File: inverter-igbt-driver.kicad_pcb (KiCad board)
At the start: 2 copper layers, 79 x 32 mm, 36 parts, among them J1 Conn_01x06, U1 NE555, U2 IXDF604SIA, U3 FOD8316, U6 Transformer_2P_2S

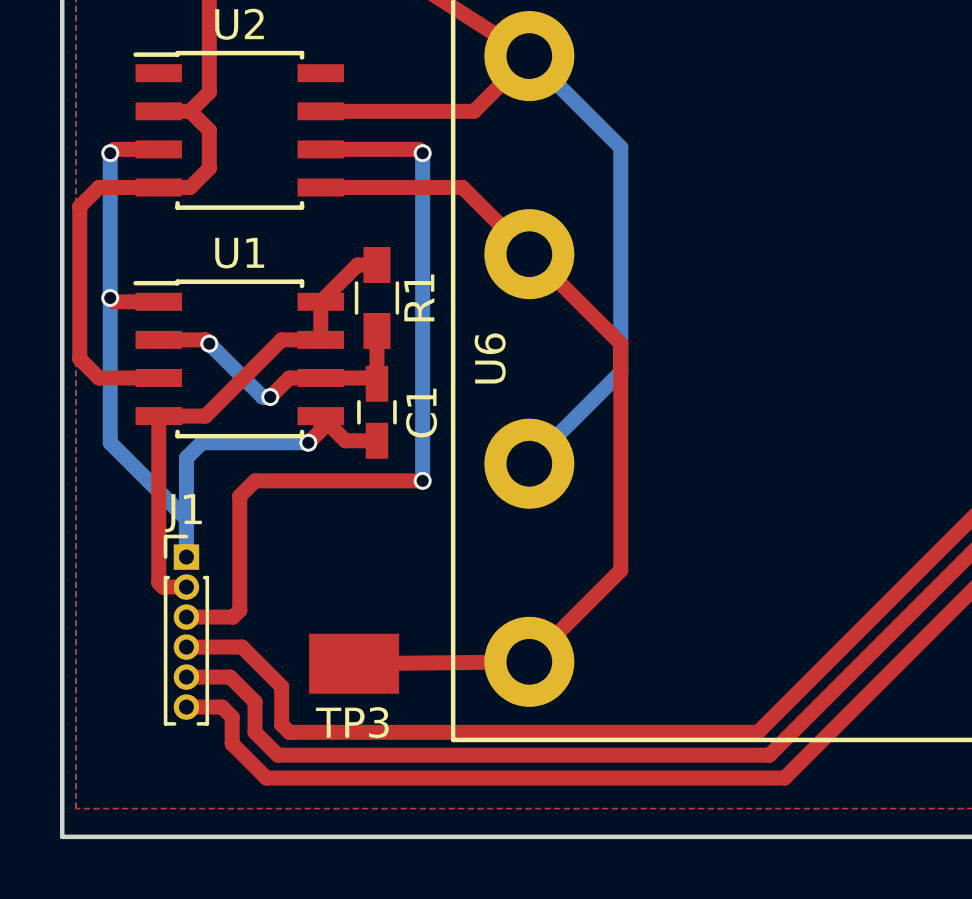
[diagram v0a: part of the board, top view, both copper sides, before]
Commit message: Adds pull-down resistors for logic nets.
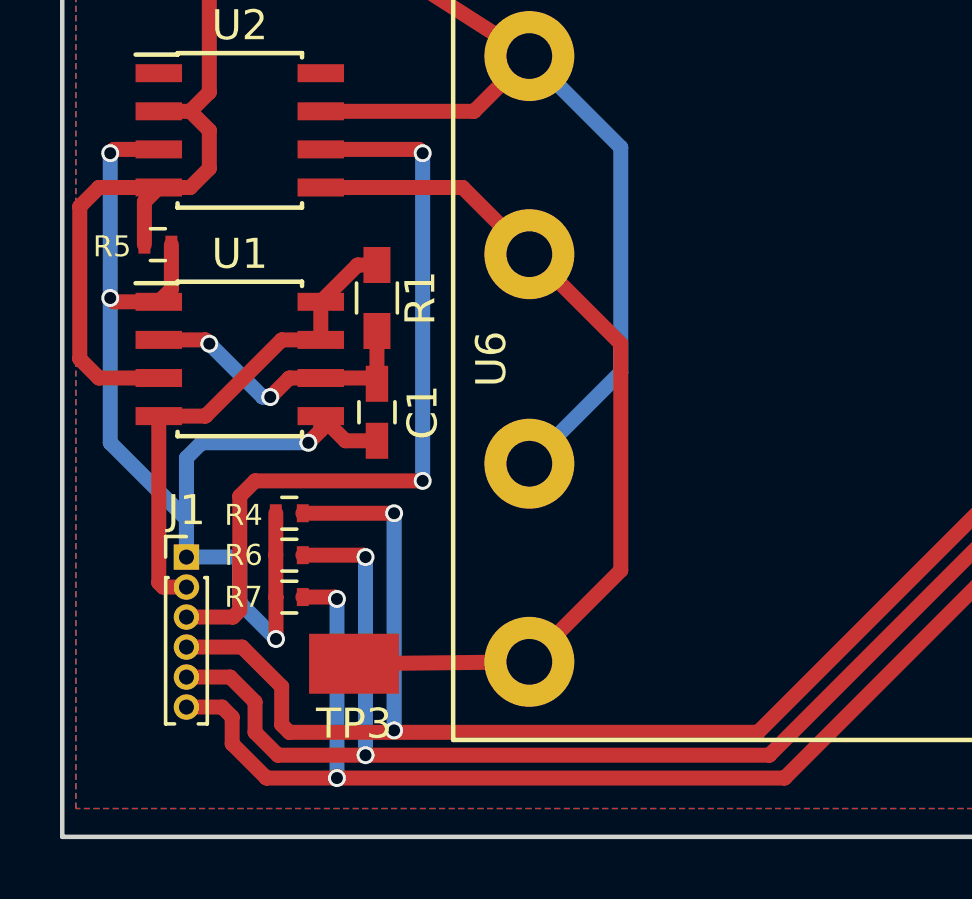
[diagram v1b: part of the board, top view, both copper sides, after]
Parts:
- added R4: 1k, Resistors_SMD:R_0402, F.Cu at (107.6, 57.2)
- added R5: 1k, Resistors_SMD:R_0402, F.Cu at (103.2, 48.3)
- added R6: 1k, Resistors_SMD:R_0402, F.Cu at (107.6, 58.6)
- added R7: 1k, Resistors_SMD:R_0402, F.Cu at (107.6, 60.0)
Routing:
- net GND: track 41.1 -> 52.4 mm, vias 6 -> 7
- net /VIN: track 59.9 -> 70.3 mm, vias 0 -> 2
- net /FAULT: track 59.0 -> 67.7 mm, vias 0 -> 2
- net /RESET: track 58.0 -> 65.3 mm, vias 2 -> 4
- net Net-(R5-Pad1): track 23.1 -> 25.2 mm

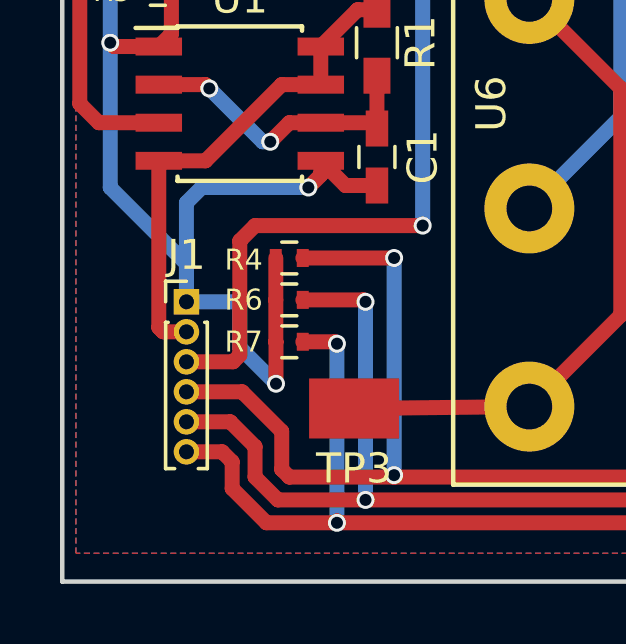
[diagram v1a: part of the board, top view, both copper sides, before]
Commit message: Add GND test point.
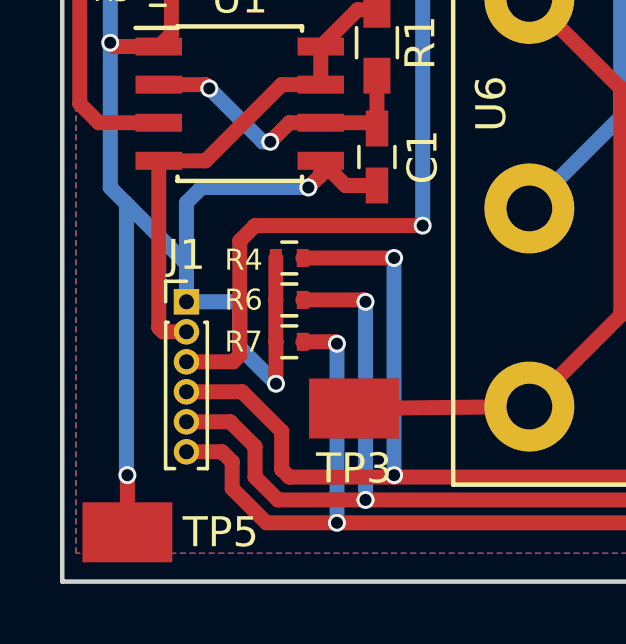
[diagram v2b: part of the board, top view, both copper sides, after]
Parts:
- added TP5: TEST, inverter-igbt-driver:TP RCT (0805), F.Cu at (102.2, 66.4)
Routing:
- net GND: track 52.4 -> 63.4 mm, vias 7 -> 8
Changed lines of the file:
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@@
 (kicad_pcb (version 4) (host pcbnew 4.0.7)
   (general
-    (links 80)
+    (links 81)
     (no_connects 2)
     (area 99.924999 35.924999 179.075001 68.075001)
     (thickness 1.6)
     (drawings 4)
-    (tracks 220)
+    (tracks 225)
     (zones 0)
-    (modules 40)
+    (modules 41)
     (nets 26)
   )
@@
     )
   )
+  (module "inverter-igbt-driver:TP RCT (0805)" (layer F.Cu)
+    (at 102.1715 66.3575)
+    (fp_text reference TP5 (at 3.1115 0) (layer F.SilkS)
+      (effects (font (size 1 1) (thickness 0.15)))
+    )
+    (fp_text value TEST (at 0 -2.25) (layer F.Fab) hide
+      (effects (font (size 1 1) (thickness 0.15)))
+    )
+    (pad 1 smd rect (at 0 0) (size 3 2) (layers F.Cu F.Paste F.Mask)
+      (net 2 GND))
+  )
   (gr_line (start 100 68) (end 100 36) (angle 90) (layer Edge.Cuts) (width 0.15))
   (gr_line (start 179 68) (end 100 68) (angle 90) (layer Edge.Cuts) (width 0.15))
@@
   (segment (start 110.49 51.138) (end 110.49 52.898) (width 0.5) (layer F.Cu) (net 1))
   (segment (start 110.49 52.898) (end 110.297 52.705) (width 0.5) (layer F.Cu) (net 1))
+  (segment (start 102.1715 66.3575) (end 102.1715 64.4525) (width 0.5) (layer F.Cu) (net 2) (status 400000))
+  (segment (start 102.13975 64.42075) (end 102.13975 55.40375) (width 0.5) (layer B.Cu) (net 2))
+  (segment (start 102.1715 64.4525) (end 102.13975 64.42075) (width 0.5) (layer B.Cu) (net 2))
+  (via (at 102.1715 64.4525) (size 0.6) (drill 0.4) (layers F.Cu B.Cu) (net 2))
   (segment (start 103.6375 48.26) (end 103.6375 49.7455) (width 0.5) (layer F.Cu) (net 2))
   (segment (start 103.6375 49.7455) (end 103.218 50.165) (width 0.5) (layer F.Cu) (net 2))
@@
   (segment (start 104.14 58.674) (end 104.14 57.404) (width 0.5) (layer B.Cu) (net 2))
   (segment (start 101.6 54.864) (end 101.6 50.038) (width 0.5) (layer B.Cu) (net 2))
-  (segment (start 104.14 57.404) (end 101.6 54.864) (width 0.5) (layer B.Cu) (net 2))
+  (segment (start 104.14 57.404) (end 102.13975 55.40375) (width 0.5) (layer B.Cu) (net 2))
+  (segment (start 102.13975 55.40375) (end 101.6 54.864) (width 0.5) (layer B.Cu) (net 2))
   (segment (start 103.218 50.165) (end 101.727 50.165) (width 0.5) (layer F.Cu) (net 2))
   (via (at 101.6 50.038) (size 0.6) (drill 0.4) (layers F.Cu B.Cu) (net 2))

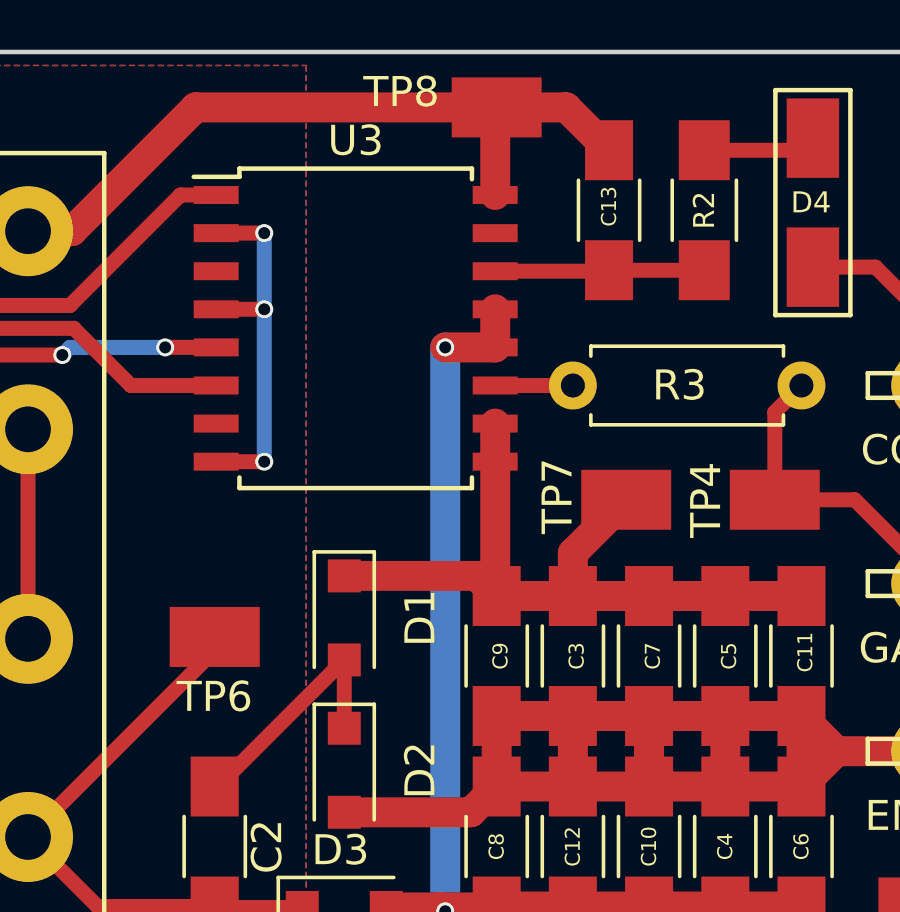
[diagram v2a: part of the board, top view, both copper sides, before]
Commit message: Fix emitter connection.
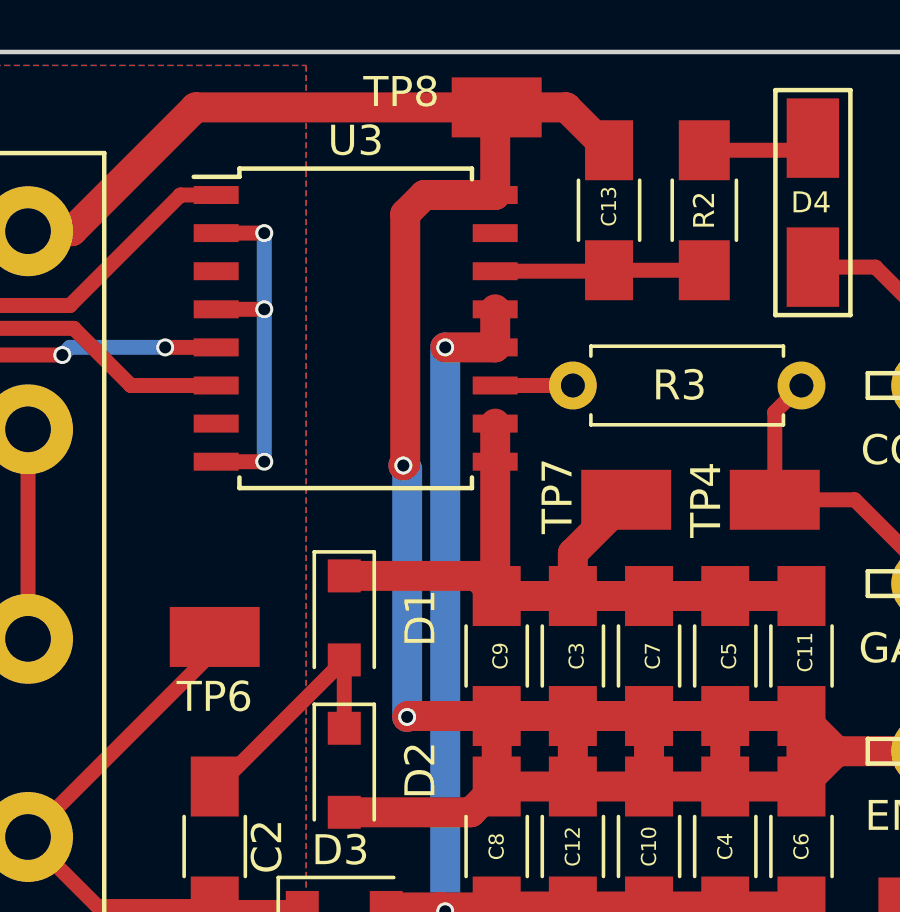
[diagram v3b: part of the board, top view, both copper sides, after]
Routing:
- net /VE_IGBT: track 68.5 -> 91.6 mm, vias 0 -> 2
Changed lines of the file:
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@@
   (general
     (links 81)
-    (no_connects 2)
+    (no_connects 1)
     (area 99.924999 35.924999 179.075001 68.075001)
     (thickness 1.6)
     (drawings 4)
-    (tracks 225)
+    (tracks 235)
     (zones 0)
     (modules 41)
@@
   (segment (start 166.751 54.134) (end 169.291 54.134) (width 1) (layer F.Cu) (net 5))
   (segment (start 169.291 54.134) (end 171.831 54.134) (width 1) (layer F.Cu) (net 5))
+  (segment (start 161.622 40.767) (end 159.258 40.767) (width 1) (layer F.Cu) (net 6) (status 400000))
+  (segment (start 158.7185 58.134) (end 161.671 58.134) (width 1) (layer F.Cu) (net 6) (status 800000))
+  (segment (start 158.6865 58.166) (end 158.7185 58.134) (width 1) (layer F.Cu) (net 6))
+  (via (at 158.6865 58.166) (size 0.6) (drill 0.4) (layers F.Cu B.Cu) (net 6))
+  (segment (start 158.6865 49.911) (end 158.6865 58.166) (width 1) (layer B.Cu) (net 6))
+  (segment (start 158.5595 49.784) (end 158.6865 49.911) (width 1) (layer B.Cu) (net 6))
+  (via (at 158.5595 49.784) (size 0.6) (drill 0.4) (layers F.Cu B.Cu) (net 6))
+  (segment (start 158.623 49.7205) (end 158.5595 49.784) (width 1) (layer F.Cu) (net 6))
+  (segment (start 158.623 41.402) (end 158.623 49.7205) (width 1) (layer F.Cu) (net 6))
+  (segment (start 159.258 40.767) (end 158.623 41.402) (width 1) (layer F.Cu) (net 6))
   (segment (start 161.671 37.846) (end 163.9885 37.846) (width 1) (layer F.Cu) (net 6))
   (segment (start 163.9885 37.846) (end 165.4175 39.275) (width 1) (layer F.Cu) (net 6))

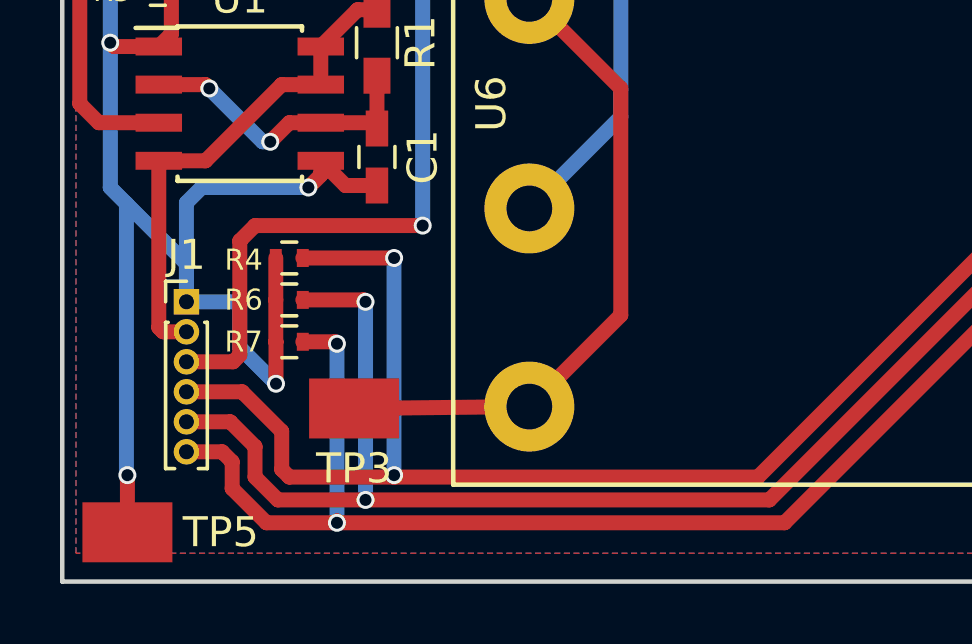
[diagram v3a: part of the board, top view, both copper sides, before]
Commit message: Switching pull-down to pull-up resistors for fault/reset.
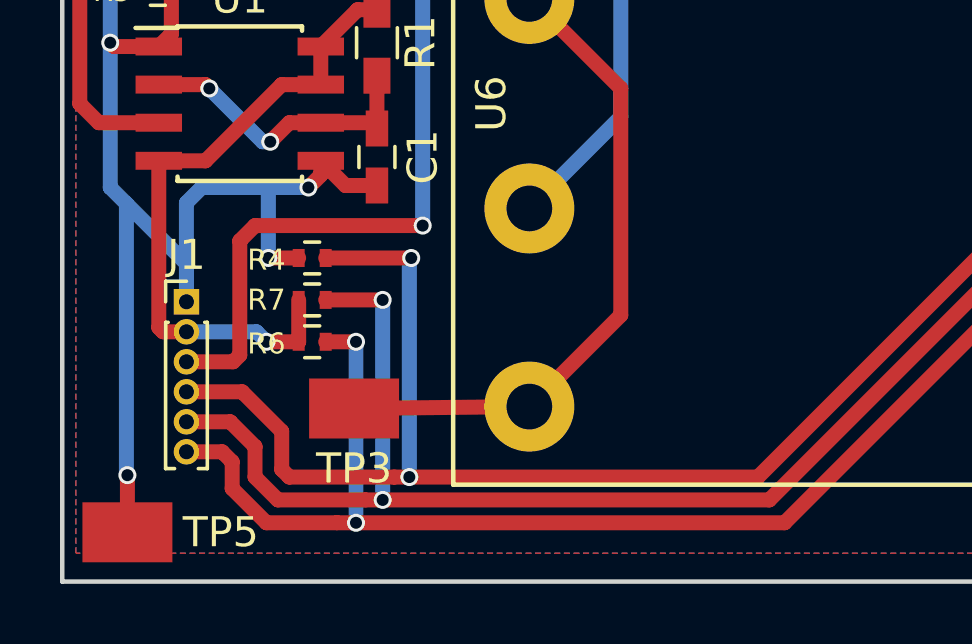
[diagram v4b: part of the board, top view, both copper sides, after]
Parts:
- moved R6 1.59 mm to (108.3, 60.0), turned to 0 degrees
- moved R7 1.59 mm to (108.3, 58.6), turned to 0 degrees
- moved R4 0.76 mm to (108.3, 57.2)
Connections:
- R6 pad 1: /FAULT -> +5V
- R6 pad 2: GND -> /RESET
- R7 pad 1: /RESET -> +5V
- R7 pad 2: GND -> /FAULT
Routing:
- net GND: track 63.4 -> 57.5 mm
- net +5V: track 16.6 -> 21.9 mm, vias 0 -> 1

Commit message: Refactor into schematic.
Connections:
- net /VDD_IGBT renamed /positive/VDD_IGBT
- net /VSS_IGBT renamed /positive/VSS_IGBT
- C10 pad 1: /VE_IGBT -> /EMIT
- C11 pad 2: /VE_IGBT -> /EMIT
- C12 pad 1: /VE_IGBT -> /EMIT
- C13 pad 1: /VE_IGBT -> /EMIT
- C3 pad 2: /VE_IGBT -> /EMIT
- C4 pad 1: /VE_IGBT -> /EMIT
- C5 pad 2: /VE_IGBT -> /EMIT
- C6 pad 1: /VE_IGBT -> /EMIT
- C7 pad 2: /VE_IGBT -> /EMIT
- C8 pad 1: /VE_IGBT -> /EMIT
- C9 pad 2: /VE_IGBT -> /EMIT
- D2 pad 2: /VE_IGBT -> /EMIT
- D4 pad 1: Net-(COLL1-Pad1) -> /COLL
- R3 pad 1: Net-(GATE1-Pad1) -> /GATE
- TP4 pad 1: Net-(GATE1-Pad1) -> /GATE
- TP8 pad 1: /VE_IGBT -> /EMIT
- U3 pad 16: /VE_IGBT -> /EMIT
- U6 pad 5: /VE_IGBT -> /EMIT
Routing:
- net /VE_IGBT: track 91.6 -> 3.02 mm, vias 2 -> 0
- net /EMIT: track 0.00 -> 88.5 mm, vias 0 -> 2
- net /GATE: track 0.00 -> 6.85 mm
- net Net-(GATE1-Pad1): track 10.6 -> 3.79 mm
- net Net-(COLL1-Pad1): track 6.75 -> 2.22 mm
- net /COLL: track 0.00 -> 4.52 mm

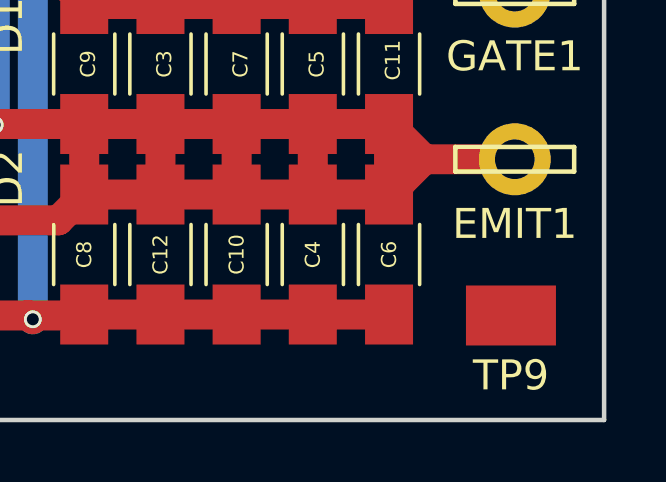
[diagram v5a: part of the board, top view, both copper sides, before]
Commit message: Fix test point connection.
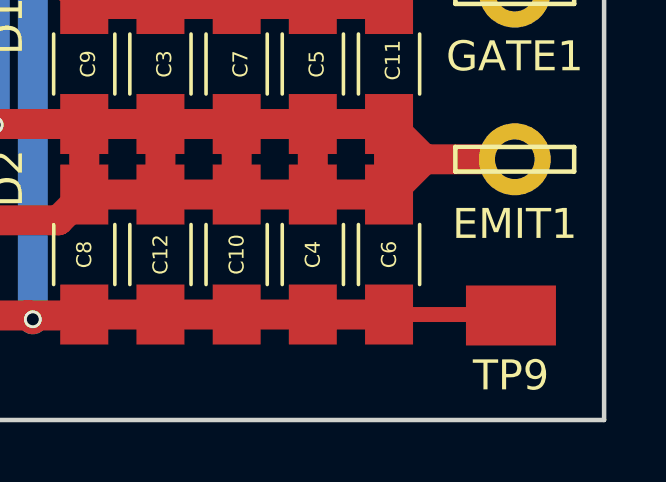
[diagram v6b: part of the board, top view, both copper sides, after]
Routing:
- net /positive/VDD_IGBT: track 35.8 -> 39.9 mm
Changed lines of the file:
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@@
   (general
     (links 78)
-    (no_connects 1)
+    (no_connects 0)
     (area 99.924999 35.924999 179.075001 68.075001)
     (thickness 1.6)
     (drawings 4)
-    (tracks 235)
+    (tracks 237)
     (zones 0)
     (modules 41)
@@
   (segment (start 166.751 58.134) (end 169.291 58.134) (width 1) (layer F.Cu) (net 25))
   (segment (start 169.291 58.134) (end 171.831 58.134) (width 1) (layer F.Cu) (net 25))
+  (segment (start 171.831 64.484) (end 175.863 64.484) (width 0.5) (layer F.Cu) (net 26) (status C00000))
+  (segment (start 175.863 64.484) (end 175.895 64.516) (width 0.5) (layer F.Cu) (net 26) (status C00000))
   (segment (start 161.622 45.847) (end 159.9565 45.847) (width 1) (layer F.Cu) (net 26))
   (segment (start 159.8295 64.516) (end 159.766 64.516) (width 1) (layer F.Cu) (net 26))
